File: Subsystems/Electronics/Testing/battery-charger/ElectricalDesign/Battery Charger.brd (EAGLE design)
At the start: 100 x 80 mm, 0 parts

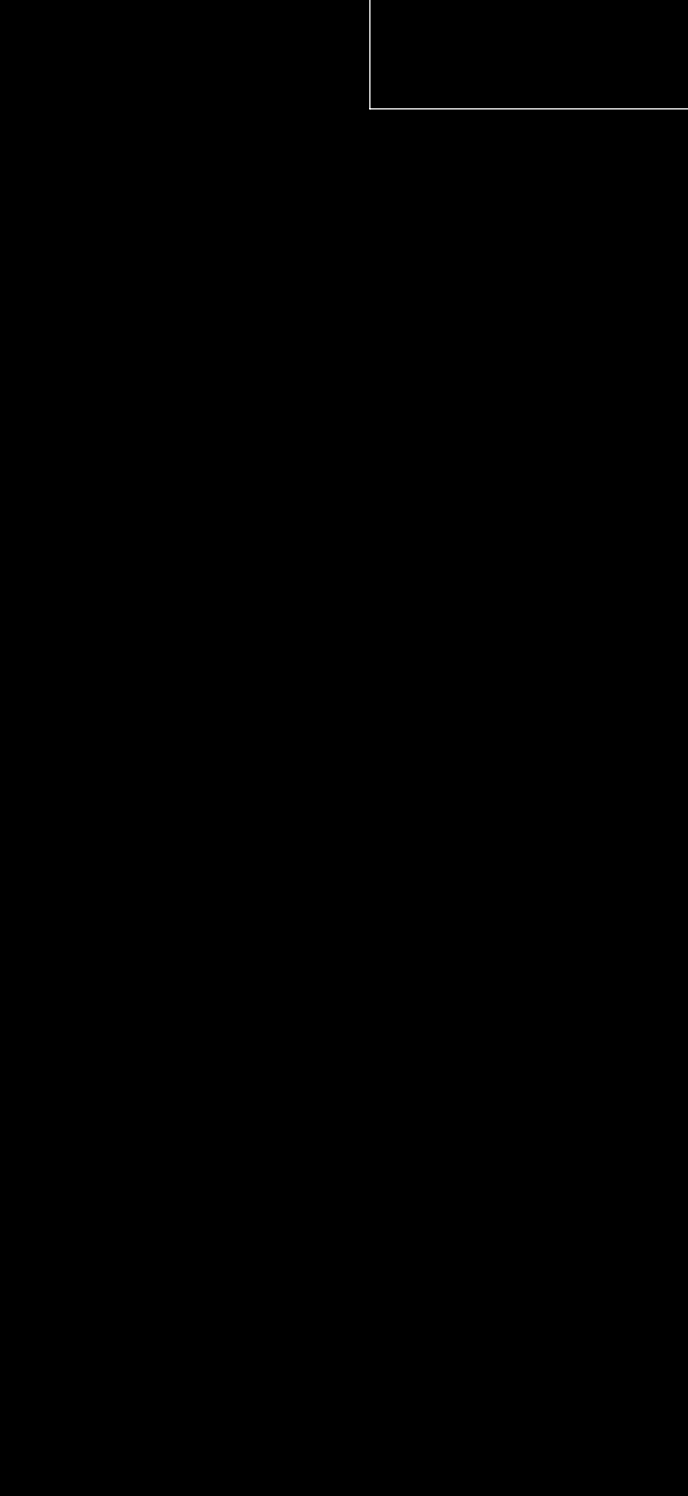
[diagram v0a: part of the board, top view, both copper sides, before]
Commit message: General Battery Charger Schematic
Majority of components placed, absent items not in CIS components library. Many labels missing.
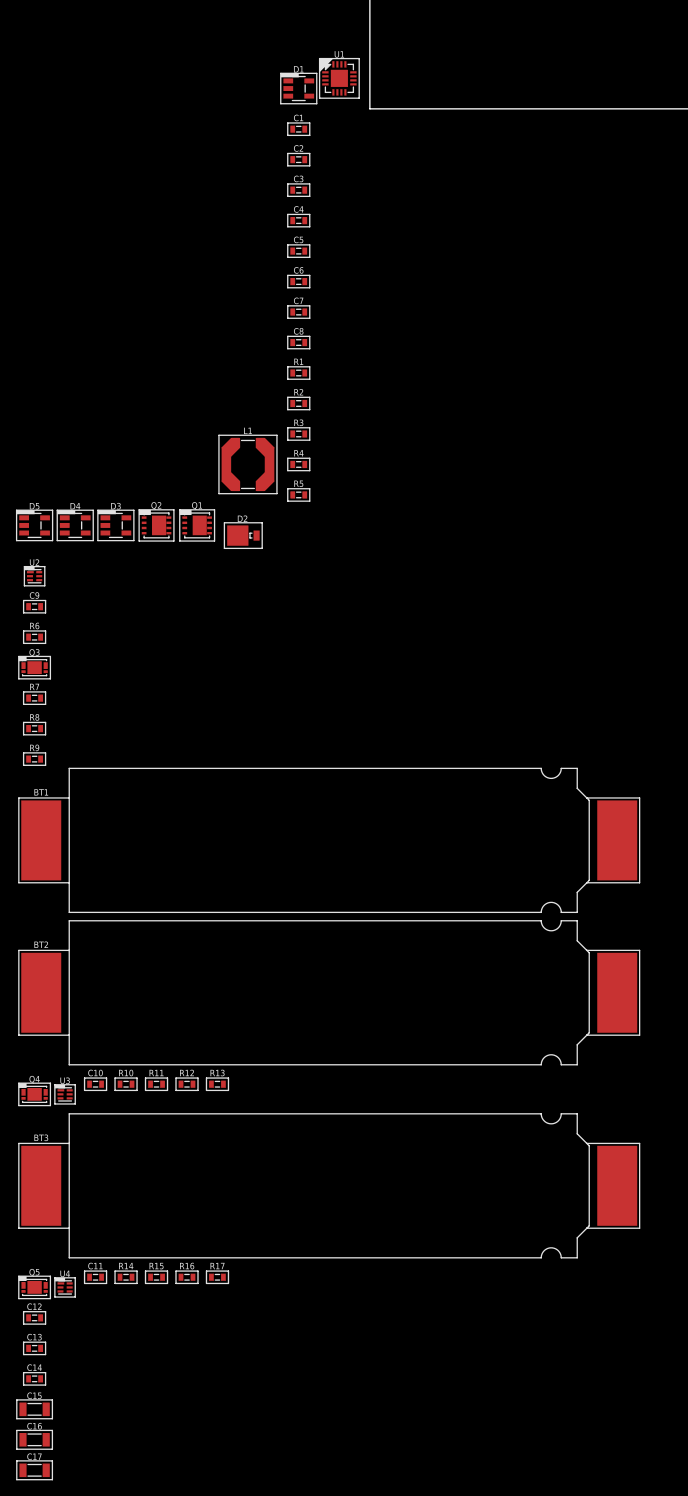
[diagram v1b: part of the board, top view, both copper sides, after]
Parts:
- added BT1, BT2, BT3: Li-Ion, CougsInSpace-Energy:18650-SOLDERED
- added C1, C12, C13, C14, C2, C3: 1µF 10%, CougsInSpace-Capacitors:1608
- added C10, C11, C4, C6, C9: 100nF 10%, CougsInSpace-Capacitors:1608
- added C15, C16, C17: 4.7µF 10%, CougsInSpace-Capacitors:3216
- added C5: 10µF 10%, CougsInSpace-Capacitors:1608
- added C7: 4.7pF ±0.1, CougsInSpace-Capacitors:1608
- added C8: 22pF 5%, CougsInSpace-Capacitors:1608
- added D1, D3, D4, D5: LTC4411, CougsInSpace-DiscreteSemi:SOT23-5
- added D2: MBRM120LT, CougsInSpace-DiscreteSemi:POWERMITE
- added L1: 10µH 20%, CougsInSpace-Coils:6060
- added Q1, Q2: CSD16406Q3, CougsInSpace-DiscreteSemi:SON-3333
- added Q3, Q4, Q5: DMN2008LFU, CougsInSpace-DiscreteSemi:UDFN-6-B
- added R1, R2: 10kΩ 0.1%, CougsInSpace-Resistors:1608
- added R10, R14, R6: 330Ω 1%, CougsInSpace-Resistors:1608
- added R11, R12, R15, R16, R7, R8: 4.75MΩ 1%, CougsInSpace-Resistors:1608
- added R13, R17, R9: 2.2kΩ 1%, CougsInSpace-Resistors:1608
- added R3: 10Ω 5%, CougsInSpace-Resistors:1608
- added R4: 47kΩ 0.1%, CougsInSpace-Resistors:1608
- added R5: 20kΩ 0.5%, CougsInSpace-Resistors:1608
- added U1: BQ24650, CougsInSpace-IC-Power:QFN-16-3535
- added U2, U3, U4: BQ29700, CougsInSpace-IC-Power:WSON-6
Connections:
- new net 5.0V: D1.1
- new net N$1: C2.1, U1.6, U1.7
- new net N$10: Q1.4, U1.15
- new net N$11: R4.1, R5.2, U1.2
- new net N$12: Q2.4, U1.13
- new net N$13: R9.2, U2.6
- new net N$14: R13.2, U3.6
- new net N$15: C12.1, C13.1, C14.1, D3.1, D4.1, D5.1
- new net N$16: Q3.3, R8.2, U2.2
- new net N$17: Q3.4, R7.2, U2.3
- new net N$18: BT1.A, C9.2, Q3.6, R7.1, U2.4
- new net N$19: Q4.3, R12.2, U3.2
- new net N$2: C1.1, R3.1, U1.1
- new net N$20: C9.1, R6.1, U2.5
- new net N$21: BT1.C, C15.1, D3.5, R6.2
- new net N$22: Q4.4, R11.2, U3.3
- new net N$23: BT2.A, C10.2, Q4.6, R11.1, U3.4
- new net N$24: C10.1, R10.1, U3.5
- new net N$25: BT2.C, C16.1, D4.5, R10.2
- new net N$26: R17.2, U4.6
- new net N$27: Q5.3, R16.2, U4.2
- new net N$28: Q5.4, R15.2, U4.3
- new net N$29: BT3.A, C11.2, Q5.6, R15.1, U4.4
- new net N$3: C3.1, D2.A, U1.12
- new net N$30: C11.1, R14.1, U4.5
- new net N$31: BT3.C, C17.1, D5.5, R14.2
- new net N$4: C4.2, L1.1, Q1.1, Q1.2, Q1.3, Q2.5, Q2.6, Q2.7, Q2.8, Q2.PAD, U1.14
- new net N$5: C4.1, D2.C, U1.16
- new net N$6: C5.1, D1.5, Q1.5, Q1.6, Q1.7, Q1.8, Q1.PAD, R3.2, R4.2
- new net N$7: C6.1, L1.2, U1.10
- new net N$8: C6.2, C7.1, C8.1, R1.2, U1.9
- new net N$9: C8.2, R1.1, R2.2, U1.8
- new net PGND: C1.2, C12.2, C13.2, C14.2, C15.2, C16.2, C17.2, C2.2, C3.2, C5.2, C7.2, D1.2, D3.2, D4.2, D5.2, Q2.1, Q2.2, Q2.3, Q3.1, Q4.1, Q5.1, R12.1, R13.1, R16.1, R17.1, R2.1, R5.1, R8.1, R9.1, U1.11, U1.PAD

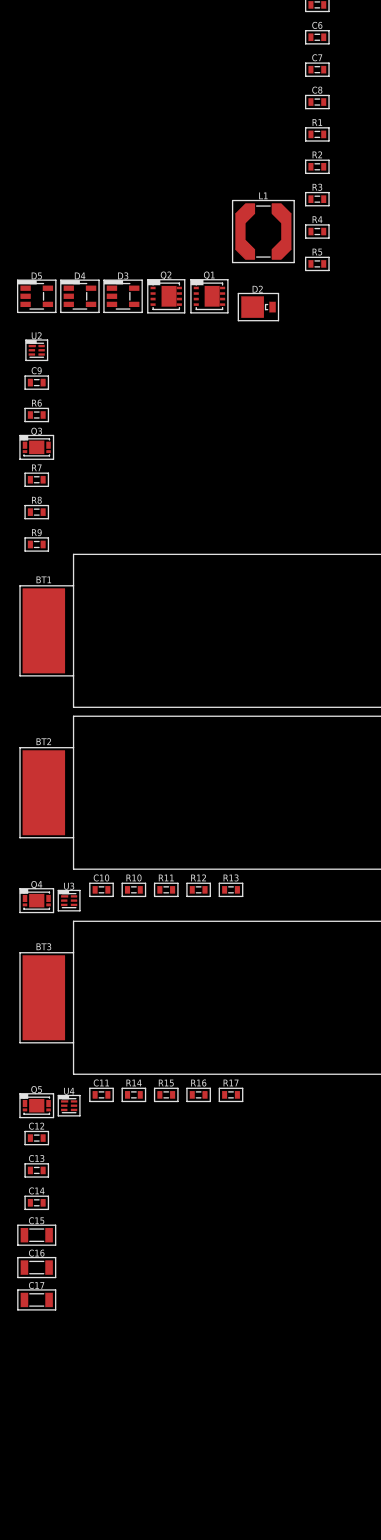
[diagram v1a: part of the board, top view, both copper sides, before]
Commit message: Partial changes
1/22/23
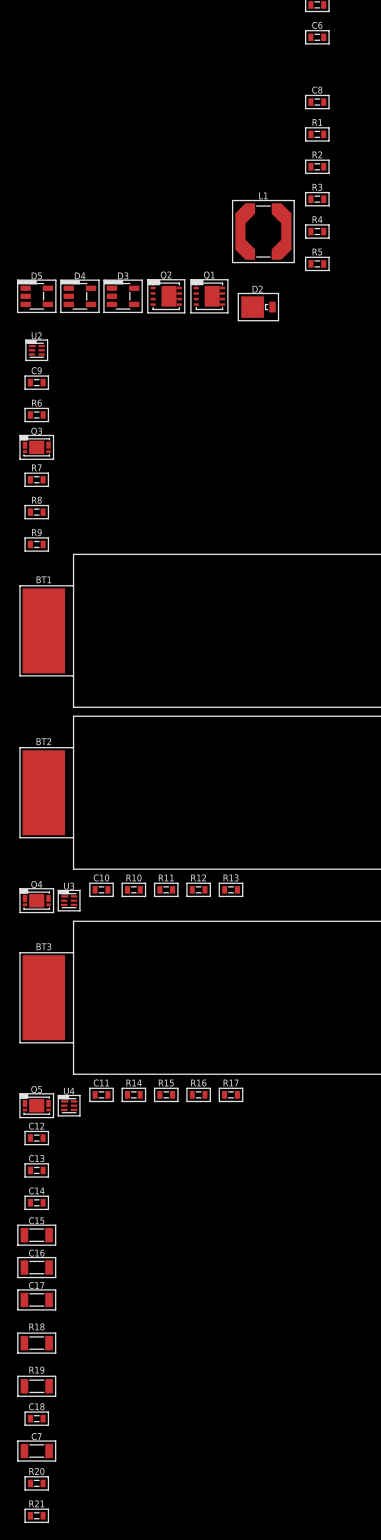
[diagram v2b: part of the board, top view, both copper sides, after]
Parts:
- added C18: 10µF 10%, CougsInSpace-Capacitors:1608
- added R18, R19: 10mΩ 1%, CougsInSpace-Resistors:3216
- added R20, R21: 0Ω <20mΩ, CougsInSpace-Resistors:1608
- C7: value 4.7pF ±0.1 -> 4.7µF 10%; device CougsInSpace-Capacitors:1608 -> CougsInSpace-Capacitors:3216
- moved C7 165.9 mm to (-41.9, -188.0)
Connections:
- new net CHARGER-SWITCHING: C12.1, C13.1, C14.1, C18.1, C6.2, C7.1, C8.1, D3.1, D4.1, D5.1, R1.2, R19.2, U1.9
- new net N$32: R2.2, R21.1
- net N$15: now also R1.1, R20.2; no longer C12.1, C13.1, C14.1, D3.1, D4.1, D5.1
- net N$7: now also R18.1
- net N$8: now also R18.2, R19.1; no longer C6.2, C7.1, C8.1, R1.2, U1.9
- net N$9: now also R20.1, R21.2; no longer R1.1, R2.2
- net PGND: now also C18.2

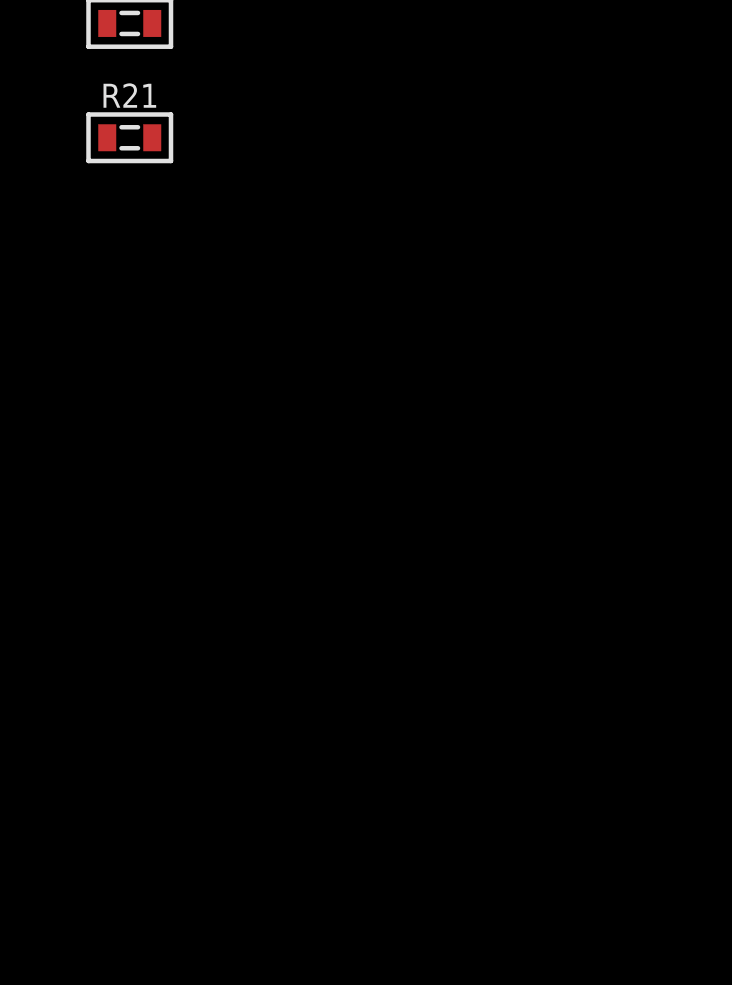
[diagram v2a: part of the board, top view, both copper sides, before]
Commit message: Added new blocks, still missing some components
No pages fully complete
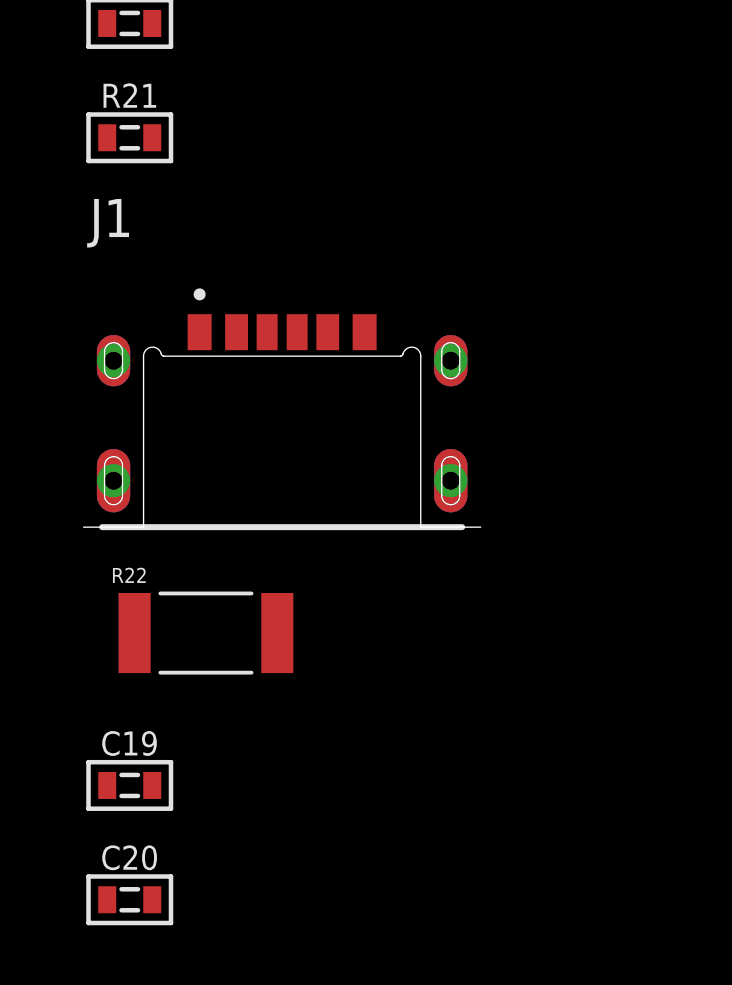
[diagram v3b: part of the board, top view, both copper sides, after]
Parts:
- added C19, C20: 1µF 10%, CougsInSpace-Capacitors:1608
- added J1: USB4515-GF-A_REVA, USB4515-GF-A_REVA:GCT_USB4515-GF-A_REVA
- added R22: CRGH2010J2R0, CRGH2010J2R0:RESC5025X65N
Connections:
- net 5.0V: now also J1.A9, J1.B9, R22.2
- net PGND: now also J1.A12, J1.B12, J1.S1, J1.S2, J1.S3, J1.S4
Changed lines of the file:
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@@
 <attribute name="TEMP" value="70°C Max 2A" x="-41.91" y="-195.58" size="1.778" layer="27" display="off"/>
+</element>
+<element name="J1" library="USB4515-GF-A_REVA" package="GCT_USB4515-GF-A_REVA" value="USB4515-GF-A_REVA" x="-36.83" y="-207.01" smashed="yes">
+<attribute name="AVAILABILITY" value="In Stock" x="-36.83" y="-207.01" size="1.778" layer="27" display="off"/>
+<attribute name="DESCRIPTION" value=" Type C USB Charging Connector " x="-36.83" y="-207.01" size="1.778" layer="27" display="off"/>
+<attribute name="MF" value="Global Connector Technology" x="-36.83" y="-207.01" size="1.778" layer="27" display="off"/>
+<attribute name="MP" value="USB4515-GF-A" x="-36.83" y="-207.01" size="1.778" layer="27" display="off"/>
+<attribute name="NAME" x="-43.25" y="-198.89" size="1.27" layer="25"/>
+<attribute name="PACKAGE" value="None" x="-36.83" y="-207.01" size="1.778" layer="27" display="off"/>
+<attribute name="PRICE" value="None" x="-36.83" y="-207.01" size="1.778" layer="27" display="off"/>
+<attribute name="PURCHASE-URL" value="https://pricing.snapeda.com/search/part/USB4515-GF-A/?ref=eda" x="-36.83" y="-207.01" size="1.778" layer="27" display="off"/>
+<attribute name="VALUE" x="-43.25" y="-199.18" size="1.27" layer="27" align="top-left"/>
+</element>
+<element name="R22" library="CRGH2010J2R0" package="RESC5025X65N" value="CRGH2010J2R0" x="-39.37" y="-212.09" smashed="yes">
+<attribute name="AVAILABILITY" value="In Stock" x="-39.37" y="-212.09" size="1.778" layer="27" display="off"/>
+<attribute name="COMMENT" value="1879499-8" x="-39.37" y="-212.09" size="1.778" layer="27" display="off"/>
+<attribute name="DESCRIPTION" value=" Res Thick Film 2010 2 Ohm 5% 1W ±200ppm/°C Molded SMD SMD T/R " x="-39.37" y="-212.09" size="1.778" layer="27" display="off"/>
+<attribute name="EU_ROHS_COMPLIANCE" value="Compliant with Exemptions" x="-39.37" y="-212.09" size="1.778" layer="27" display="off"/>
+<attribute name="MF" value="TE Connectivity" x="-39.37" y="-212.09" size="1.778" layer="27" display="off"/>
+<attribute name="MP" value="CRGH2010J2R0" x="-39.37" y="-212.09" size="1.778" layer="27" display="off"/>
+<attribute name="NAME" x="-42.53" y="-210.42" size="0.5" layer="25"/>
+<attribute name="PACKAGE" value="2010" x="-39.37" y="-212.09" size="1.778" layer="27" display="off"/>
+<attribute name="PRICE" value="None" x="-39.37" y="-212.09" size="1.778" layer="27" display="off"/>
+<attribute name="PURCHASE-URL" value="https://pricing.snapeda.com/search/part/CRGH2010J2R0/?ref=eda" x="-39.37" y="-212.09" size="1.778" layer="27" display="off"/>
+<attribute name="VALUE" x="-42.53" y="-213.76" size="0.5" layer="27" align="top-left"/>
+</element>
+<element name="C19" library="CougsInSpace-Capacitors" package="1608" value="1µF 10%" x="-41.91" y="-217.17" smashed="yes">
+<attribute name="NAME" x="-41.91" y="-215.77" size="0.8" layer="25" font="vector" ratio="15" align="center"/>
+<attribute name="PACKAGE" value="1608" x="-41.91" y="-217.17" size="1.778" layer="27" display="off"/>
+<attribute name="SKU" value="11-105A" x="-41.91" y="-217.17" size="1.778" layer="27" display="off"/>
+<attribute name="TEMP" value="X5R" x="-41.91" y="-217.17" size="1.778" layer="27" display="off"/>
+<attribute name="VOLTAGE" value="6.3V" x="-41.91" y="-217.17" size="1.778" layer="27" display="off"/>
+</element>
+<element name="C20" library="CougsInSpace-Capacitors" package="1608" value="1µF 10%" x="-41.91" y="-220.98" smashed="yes">
+<attribute name="NAME" x="-41.91" y="-219.58" size="0.8" layer="25" font="vector" ratio="15" align="center"/>
+<attribute name="PACKAGE" value="1608" x="-41.91" y="-220.98" size="1.778" layer="27" display="off"/>
+<attribute name="SKU" value="11-105A" x="-41.91" y="-220.98" size="1.778" layer="27" display="off"/>
+<attribute name="TEMP" value="X5R" x="-41.91" y="-220.98" size="1.778" layer="27" display="off"/>
+<attribute name="VOLTAGE" value="6.3V" x="-41.91" y="-220.98" size="1.778" layer="27" display="off"/>
 </element>
 </elements>
@@
 <contactref element="C18" pad="2"/>
 <contactref element="C7" pad="2"/>
+<contactref element="J1" pad="A12"/>
+<contactref element="J1" pad="B12"/>
+<contactref element="J1" pad="S1"/>
+<contactref element="J1" pad="S2"/>
+<contactref element="J1" pad="S4"/>
+<contactref element="J1" pad="S3"/>
+<wire x1="-42.45" y1="-203.01" x2="-42.45" y2="-207.01" width="0" layer="19" extent="1-1"/>
+<wire x1="-39.58" y1="-202.06" x2="-42.45" y2="-203.01" width="0" layer="19" extent="1-1"/>
+<wire x1="-34.08" y1="-202.06" x2="-39.58" y2="-202.06" width="0" layer="19" extent="1-1"/>
+<wire x1="-31.21" y1="-203.01" x2="-34.08" y2="-202.06" width="0" layer="19" extent="1-1"/>
+<wire x1="-31.21" y1="-207.01" x2="-31.21" y2="-203.01" width="0" layer="19" extent="1-1"/>
+<wire x1="-40.46" y1="-187.96" x2="-39.58" y2="-202.06" width="0" layer="19" extent="1-1"/>
 <wire x1="-41.16" y1="-184.15" x2="-40.46" y2="-187.96" width="0" layer="19" extent="1-1"/>
 <wire x1="-40.46" y1="-170.18" x2="-41.16" y2="-184.15" width="0" layer="19" extent="1-1"/>
@@
 <wire x1="-3.56" y1="2.06" x2="-4.06" y2="2.06" width="0" layer="19" extent="1-1"/>
 </signal>
-<signal name="N$2">
-<contactref element="U1" pad="1"/>
-<contactref element="C1" pad="1"/>
-<contactref element="R3" pad="1"/>
-<wire x1="-9.64" y1="-2.54" x2="-9.64" y2="-40.64" width="0" layer="19" extent="1-1"/>
-<wire x1="-5.56" y1="4.56" x2="-9.64" y2="-2.54" width="0" layer="19" extent="1-1"/>
-</signal>
 <signal name="N$3">
 <contactref element="U1" pad="12"/>
@@
 <wire x1="-9.64" y1="-13.97" x2="-16.51" y2="-53.34" width="0" layer="19" extent="1-1"/>
 <wire x1="-4.56" y1="5.56" x2="-9.64" y2="-13.97" width="0" layer="19" extent="1-1"/>
-</signal>
-<signal name="5.0V">
-<contactref element="D1" pad="1"/>
 </signal>
 <signal name="N$7">
@@
 <wire x1="-3.06" y1="2.06" x2="-8.14" y2="-29.21" width="0" layer="19" extent="1-1"/>
 </signal>
-<signal name="N$6">
-<contactref element="D1" pad="5"/>
-<contactref element="R3" pad="2"/>
-<contactref element="C5" pad="1"/>
-<contactref element="R4" pad="2"/>
-<contactref element="Q1" pad="PAD"/>
-<contactref element="Q1" pad="6"/>
-<contactref element="Q1" pad="8"/>
-<contactref element="Q1" pad="7"/>
-<contactref element="Q1" pad="5"/>
-<wire x1="-20.04" y1="-52.395" x2="-21.265" y2="-52.07" width="0" layer="19" extent="1-1"/>
-<wire x1="-20.04" y1="-51.745" x2="-20.04" y2="-52.395" width="0" layer="19" extent="1-1"/>
-<wire x1="-20.04" y1="-51.095" x2="-20.04" y2="-51.745" width="0" layer="19" extent="1-1"/>
-<wire x1="-20.04" y1="-53.045" x2="-20.04" y2="-52.395" width="0" layer="19" extent="1-1"/>
-<wire x1="-8.14" y1="-44.45" x2="-20.04" y2="-51.095" width="0" layer="19" extent="1-1"/>
-<wire x1="-8.14" y1="-40.64" x2="-8.14" y2="-44.45" width="0" layer="19" extent="1-1"/>
-<wire x1="-9.64" y1="-17.78" x2="-8.14" y2="-40.64" width="0" layer="19" extent="1-1"/>
-<wire x1="-7.58" y1="3.49" x2="-9.64" y2="-17.78" width="0" layer="19" extent="1-1"/>
-</signal>
 <signal name="N$11">
 <contactref element="R4" pad="1"/>
@@
 <wire x1="-9.64" y1="-33.02" x2="-41.16" y2="-191.77" width="0" layer="19" extent="1-1"/>
 </signal>
+<signal name="5.0V">
+<contactref element="J1" pad="A9"/>
+<contactref element="J1" pad="B9"/>
+<contactref element="D1" pad="1"/>
+<contactref element="R22" pad="2"/>
+<wire x1="-38.35" y1="-202.06" x2="-36.99" y2="-212.09" width="0" layer="19" extent="1-1"/>
+<wire x1="-35.31" y1="-202.06" x2="-38.35" y2="-202.06" width="0" layer="19" extent="1-1"/>
+<wire x1="-10.2" y1="3.49" x2="-35.31" y2="-202.06" width="0" layer="19" extent="1-1"/>
+</signal>
+<signal name="N$33">
+<contactref element="R4" pad="2"/>
+<contactref element="R3" pad="2"/>
+<contactref element="C5" pad="1"/>
+<contactref element="Q1" pad="PAD"/>
+<contactref element="Q1" pad="6"/>
+<contactref element="Q1" pad="8"/>
+<contactref element="Q1" pad="7"/>
+<contactref element="Q1" pad="5"/>
+<contactref element="D1" pad="5"/>
+<wire x1="-20.04" y1="-52.395" x2="-21.265" y2="-52.07" width="0" layer="19" extent="1-1"/>
+<wire x1="-20.04" y1="-51.745" x2="-20.04" y2="-52.395" width="0" layer="19" extent="1-1"/>
+<wire x1="-20.04" y1="-51.095" x2="-20.04" y2="-51.745" width="0" layer="19" extent="1-1"/>
+<wire x1="-20.04" y1="-53.045" x2="-20.04" y2="-52.395" width="0" layer="19" extent="1-1"/>
+<wire x1="-8.14" y1="-44.45" x2="-20.04" y2="-51.095" width="0" layer="19" extent="1-1"/>
+<wire x1="-8.14" y1="-40.64" x2="-8.14" y2="-44.45" width="0" layer="19" extent="1-1"/>
+<wire x1="-9.64" y1="-17.78" x2="-8.14" y2="-40.64" width="0" layer="19" extent="1-1"/>
+<wire x1="-7.58" y1="3.49" x2="-9.64" y2="-17.78" width="0" layer="19" extent="1-1"/>
+</signal>
+<signal name="N$6">
+<contactref element="U1" pad="1"/>
+<contactref element="C1" pad="1"/>
+<contactref element="R3" pad="1"/>
+<wire x1="-9.64" y1="-2.54" x2="-9.64" y2="-40.64" width="0" layer="19" extent="1-1"/>
+<wire x1="-5.56" y1="4.56" x2="-9.64" y2="-2.54" width="0" layer="19" extent="1-1"/>
+</signal>
 </signals>
